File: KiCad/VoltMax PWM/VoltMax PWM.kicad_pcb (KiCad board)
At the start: 2 copper layers, 70 x 20 mm, 32 parts, among them IC1 DS1809Z-010+, IC2 NCV4264-2ST50T3G, J1 BAT-, J2 510-, J3 VIN+, J4 PAD_Fire2, J5 PAD_Fire1, J6 VM-, J7 VM+, Q1 SSM3J334R_LF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

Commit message: Small fixes
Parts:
- added REF**: 0.36_inch_VM, VoltMax PWM:0.36_inch_VM, F.Cu at (141.7, 100.3)
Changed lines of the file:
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@@
     (tracks 406)
     (zones 0)
-    (modules 32)
+    (modules 33)
     (nets 23)
   )
@@
     (add_net "Net-(S4-PadMH1)")
     (add_net "Net-(S4-PadMH2)")
+  )
+  (module "VoltMax PWM:0.36_inch_VM" (layer F.Cu)
+    (at 141.7 100.3)
+    (fp_text reference REF** (at 0 -2.69) (layer F.SilkS)
+      (effects (font (size 1 1) (thickness 0.15)))
+    )
+    (fp_text value 0.36_inch_VM (at 0 -0.73) (layer F.Fab) hide
+      (effects (font (size 1 1) (thickness 0.15)))
+    )
+    (fp_line (start 11.2781 -7.3084) (end -11.5219 -7.3084) (layer F.SilkS) (width 0.15))
+    (fp_line (start -11.5219 -7.3084) (end -11.5219 6.9516) (layer F.SilkS) (width 0.15))
+    (fp_line (start -11.5219 6.9516) (end 11.2781 6.9516) (layer F.SilkS) (width 0.15))
+    (fp_line (start 11.2781 6.9516) (end 11.2781 -7.3084) (layer F.SilkS) (width 0.15))
+    (model "${KIPRJMOD}/VoltMax PWM.pretty/XDxx09x3.step"
+      (offset (xyz -0.1 0.15 4.45))
+      (scale (xyz 1.018 1 1.022))
+      (rotate (xyz -90 0 0))
+    )
   )
   (module "VoltMax PWM:PSMN1R2-25YLC_115" (layer B.Cu)
@@
     (pad 1 thru_hole rect (at -1.26 0 180) (size 1.8 1.8) (drill 0.9) (layers *.Cu *.Mask)
       (net 10 /VIN+toFire1))
-    (model ${KISYS3DMOD}/LED_THT.3dshapes/LED_D4.0mm.wrl
-      (offset (xyz -1.25 0 -1.75))
-      (scale (xyz 1 1 1))
-      (rotate (xyz 0 0 0))
-    )
     (model "${KIPRJMOD}/VoltMax PWM.pretty/ELM 2.igs"
       (at (xyz 0 0 0))
       (scale (xyz 1 0.1 1))
       (rotate (xyz -90 0 90))
+    )
+    (model "${KIPRJMOD}/VoltMax PWM.pretty/SSL-LX40FT3ID-v0.step"
+      (offset (xyz 0 0 1.25))
+      (scale (xyz 1 1 1))
+      (rotate (xyz 0 0 180))
     )
   )
@@
     (tags "Tactile Switch")
     (attr smd)
-    (fp_text reference S1 (at 0 -4.25 270) (layer F.SilkS)
+    (fp_text reference S1 (at 1.856 -0.277) (layer F.SilkS)
       (effects (font (size 1 1) (thickness 0.15)))
     )
@@
   (via (at 180.4 104.4) (size 0.6) (drill 0.3) (layers F.Cu B.Cu) (net 6))
   (via (at 183.8 105.1) (size 0.6) (drill 0.3) (layers F.Cu B.Cu) (net 6))
+  (via (at 178.5 108.4) (size 0.6) (drill 0.3) (layers F.Cu B.Cu) (net 6))
+  (via (at 179.2 109.1) (size 0.6) (drill 0.3) (layers F.Cu B.Cu) (net 6))
+  (via (at 178.5 109.1) (size 0.6) (drill 0.3) (layers F.Cu B.Cu) (net 6))
+  (via (at 178.5 107.7) (size 0.6) (drill 0.3) (layers F.Cu B.Cu) (net 6))
+  (via (at 178.5 107) (size 0.6) (drill 0.3) (layers F.Cu B.Cu) (net 6))
+  (via (at 178.5 106.3) (size 0.6) (drill 0.3) (layers F.Cu B.Cu) (net 6))
+  (via (at 179.725 104.4) (size 0.6) (drill 0.3) (layers F.Cu B.Cu) (net 6))
+  (via (at 179.6 105.1) (size 0.6) (drill 0.3) (layers F.Cu B.Cu) (net 6))
   (segment (start 156.51 101.1497) (end 156.51 99.1503) (width 0.4) (layer F.Cu) (net 7))
   (segment (start 156.51 98.2001) (end 156.51 99.1503) (width 0.4) (layer F.Cu) (net 7))
@@
   (via (at 179.6 95.5) (size 0.6) (drill 0.3) (layers F.Cu B.Cu) (net 8))
   (via (at 183.8 95.5) (size 0.6) (drill 0.3) (layers F.Cu B.Cu) (net 8))
-  (via (at 178.2 108.6) (size 0.6) (drill 0.3) (layers F.Cu B.Cu) (net 6))
-  (via (at 178.9 109.3) (size 0.6) (drill 0.3) (layers F.Cu B.Cu) (net 6))
-  (via (at 178.2 109.3) (size 0.6) (drill 0.3) (layers F.Cu B.Cu) (net 6))
-  (via (at 178.2 107.9) (size 0.6) (drill 0.3) (layers F.Cu B.Cu) (net 6))
-  (via (at 178.2 107.2) (size 0.6) (drill 0.3) (layers F.Cu B.Cu) (net 6))
-  (via (at 178.2 106.5) (size 0.6) (drill 0.3) (layers F.Cu B.Cu) (net 6))
-  (via (at 179.725 104.4) (size 0.6) (drill 0.3) (layers F.Cu B.Cu) (net 6))
-  (via (at 179.6 105.1) (size 0.6) (drill 0.3) (layers F.Cu B.Cu) (net 6))
   (via (at 177.9 93) (size 0.6) (drill 0.3) (layers F.Cu B.Cu) (net 8))
   (via (at 179.3 90.9) (size 0.6) (drill 0.3) (layers F.Cu B.Cu) (net 8))

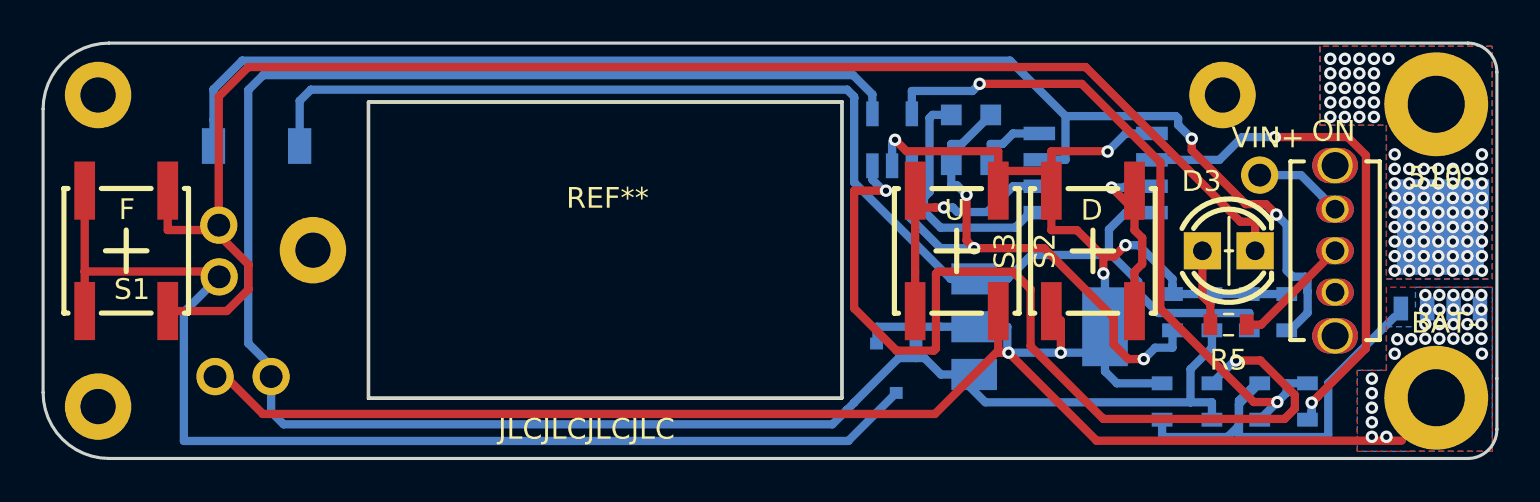
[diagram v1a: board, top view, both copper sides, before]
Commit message: Better thermal, cleaner vias/traces
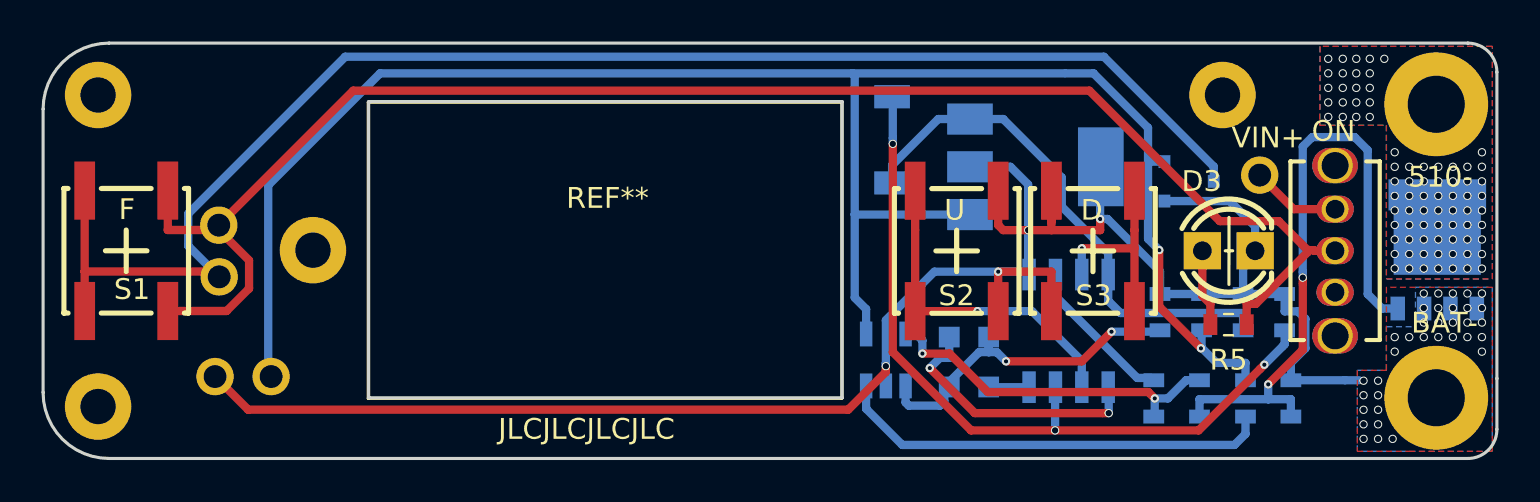
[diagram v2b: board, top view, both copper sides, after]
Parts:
- moved D2 30.6 mm to (155.4, 94.8), turned to 270 degrees
- moved Q1 16.7 mm to (169.7, 96.8), turned to 0 degrees
- moved D1 10.7 mm to (159.1, 105.5)
- moved U1 10.6 mm to (155.1, 105.4)
- moved IC1 7.71 mm to (163.9, 104.0), turned to 90 degrees
- moved IC2 7.70 mm to (162.3, 96.1)
- moved R4 7.40 mm to (168.0, 107.3), turned to 270 degrees
- moved R1 6.20 mm to (174.6, 107.3)
- moved R3 2.90 mm to (170.2, 107.3), turned to 270 degrees
- moved R2 1.62 mm to (172.4, 107.3), turned to 270 degrees
- moved C1 0.60 mm to (168.3, 103.1)
- moved C2 0.50 mm to (170.3, 103.1)
- moved C3 0.30 mm to (172.3, 103.1)
- moved Q2 0.15 mm to (181.7, 98.0)
- moved C4 0.10 mm to (174.3, 103.1)
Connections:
- D3 pad 1: /VIN+toFire1 -> GND
- J5 pad 1: /VIN+toFire1 -> /VIN+toR5
- S1 pad 1: /VIN+toFire1 -> /VIN+toR5
- S1 pad 2: /VIN+toFire1 -> /VIN+toR5
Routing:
- net /VIN+toFire1: track 73.5 -> 0.00 mm
- net /VIN+toR5: track 5.73 -> 77.1 mm
- net /5V+toC3: track 60.7 -> 25.5 mm
- net /D2toSTR: track 68.5 -> 37.0 mm, vias 2 -> 3
- net /U1toR2: track 45.0 -> 21.1 mm, vias 2 -> 0
- net GND: track 120.7 -> 98.9 mm, vias 36 -> 39
- net /POTWIPER: track 25.2 -> 7.45 mm, vias 2 -> 0
- net /U1OUT: track 32.6 -> 17.1 mm
- net /VIN+toQ1Drain: track 56.2 -> 71.5 mm
- net /VIN+fromQ1Source: track 101.6 -> 89.8 mm, vias 0 -> 2
- net Net-(C1-Pad1): track 28.0 -> 16.3 mm, vias 3 -> 2
- net Net-(Q2-Pad4): track 21.6 -> 31.2 mm, vias 0 -> 2
- net /UP: track 12.4 -> 16.1 mm
- net /POT0%: track 3.55 -> 1.92 mm
- net /POT100%: track 11.9 -> 12.9 mm, vias 0 -> 2
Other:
- net class Default: via_dia 0.6 -> 0.4
- rule trace_min: 0.2 -> 0.4

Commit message: David has spoken and changes have been made, cleaner vias/traces
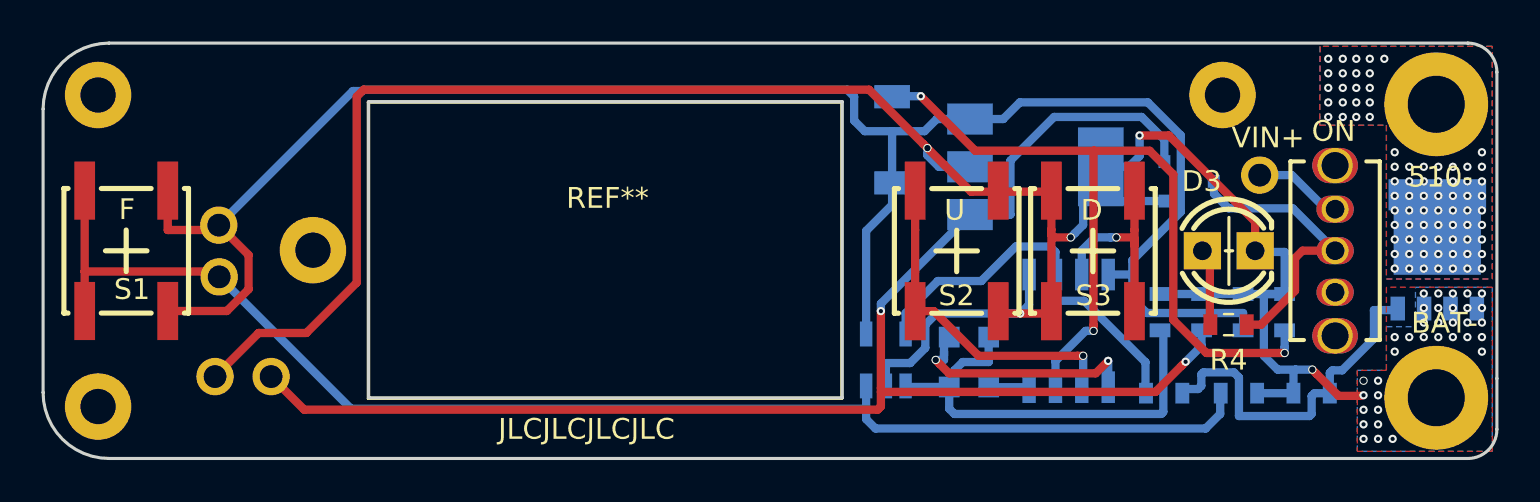
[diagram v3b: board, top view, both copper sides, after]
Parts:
- removed the R4 at (168.0, 107.3)
- R2: value 1M -> 10K
- moved R3 1.72 mm to (168.5, 107.0), turned to 0 degrees
- moved R1 1.03 mm to (175.6, 107.0), turned to 180 degrees
- moved R2 0.40 mm to (172.1, 107.0), turned to 0 degrees
- renumbered R5 to R4
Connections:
- C3 pad 1: /5V+toC3 -> /S1toVS
- D2 pad 2: /5V+toC3 -> /S1toVS
- IC1 pad 6: /POTWIPER -> /U1OUT
- IC1 pad 8: /5V+toC3 -> /S1toVS
- IC2 pad 3: /5V+toC3 -> /S1toVS
- J4 pad 1: /VIN+toQ1Drain -> /CStoR2
- J5 pad 1: /VIN+toR5 -> /S1toVS
- Q1 pad 3: /VIN+toQ1Drain -> /VIN+toR5
- R2 pad 1: /VIN+fromQ1Source -> /CStoR2
- R2 pad 2: /U1toR2 -> GND
- S1 pad 1: /VIN+toR5 -> /S1toVS
- S1 pad 2: /VIN+toR5 -> /S1toVS
- S1 pad 3: /VIN+toQ1Drain -> /CStoR2
- S1 pad 4: /VIN+toQ1Drain -> /CStoR2
- U1 pad 3: /U1toR2 -> /CStoR2
- U1 pad 4: /VIN+fromQ1Source -> /S1toVS
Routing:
- net /S1toVS: track 0.00 -> 90.9 mm
- net /VIN+toQ1Drain: track 71.5 -> 0.00 mm
- net /CStoR2: track 0.00 -> 66.4 mm
- net /VIN+toR5: track 77.1 -> 14.1 mm
- net /5V+toC3: track 25.5 -> 0.00 mm
- net /U1toR2: track 21.1 -> 0.00 mm
- net GND: track 98.9 -> 118.9 mm, vias 39 -> 40
- net /VIN+fromQ1Source: track 89.8 -> 72.5 mm
- net Net-(Q2-Pad4): track 31.2 -> 16.7 mm, vias 2 -> 0
- net /POTWIPER: track 7.45 -> 0.00 mm
- net Net-(C1-Pad1): track 16.3 -> 21.0 mm, vias 2 -> 0
- net /D2toSTR: track 37.0 -> 41.6 mm
- net /U1OUT: track 17.1 -> 18.8 mm, vias 2 -> 0
- net /POT100%: track 12.9 -> 11.7 mm
- net /R5toD3: track 3.72 -> 2.88 mm
